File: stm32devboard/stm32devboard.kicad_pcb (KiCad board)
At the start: 4 copper layers, 20.3 x 61 mm, 44 parts, among them J1 Conn_01x20, J2 Conn_01x20, J3 USB_C_Receptacle_USB2.0, J4 Conn_01x03, SW1 SW_SPST, SW2 SW_SPST, U1 STM32F042C6Tx, U2 AP63203WU, U3 TCAN332, U4 IP4234CZ6,125

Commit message: Fixed DR fixes
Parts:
- removed J4: Conn_01x03, Connector_PinHeader_2.54mm:PinHeader_1x03_P2.54mm_Vertical
- removed JP1, JP2, JP3: Jumper_2_Open, Jumper:SolderJumper-2_P1.3mm_Open_RoundedPad1.0x1.5mm
- added C15: GCM1885C2A200JA16D, Capacitor_SMD:C_0603_1608Metric, F.Cu at (142.3, 108.6)
- added C16: GCM1885C2A200JA16D, Capacitor_SMD:C_0603_1608Metric, F.Cu at (144.7, 109.4)
- added J5: Conn_ARM_JTAG_SWD_10, Connector:Tag-Connect_TC2030-IDC-NL_2x03_P1.27mm_Vertical, F.Cu at (152.2, 89.4)
- added X1: ECS-160-10-36Q-ES-TR, Crystal:Crystal_SMD_2520-4Pin_2.5x2.0mm, F.Cu at (142.4, 106.3)
- C11: value DNP -> 0.1u
- C12: value DNP -> 1n
- R2: value 1 -> 0
- R7, R8: value 120 -> 60.4
- moved C12 10.3 mm to (144.7, 81.6), turned to 180 degrees
- moved C11 7.81 mm to (154.3, 72.9), turned to -90 degrees
- moved C8 5.41 mm to (147.0, 111.6)
- moved R3 5.32 mm to (147.0, 113.1), turned to 0 degrees
- moved R2 2.33 mm to (147.0, 110.0), turned to 0 degrees
- moved R7 1.36 mm to (144.7, 83.1)
- moved R8 1.36 mm to (141.7, 83.1)
- moved R6 0.22 mm to (142.9, 94.2), turned to 90 degrees
- turned R5 to 90 degrees
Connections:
- net LED renamed Net-(U1-PA15)
- C11 pad 1: GND -> /USB_SHLD
- C11 pad 2: CAN- -> GND
- C12 pad 2: CAN+ -> Net-(C12-Pad2)
- J2 pad 2: PF0 -> GND
- J2 pad 3: PF1 -> PF11
- J2 pad 4: PF11 -> +3V3
- R5 pad 1: Net-(U3-TXD) -> PB9
- R5 pad 2: PB9 -> Net-(U3-TXD)
- R6 pad 1: Net-(U3-RXD) -> PB8
- R6 pad 2: PB8 -> Net-(U3-RXD)
- R7 pad 1: Net-(JP1-B) -> CAN-
- R7 pad 2: GND -> Net-(C12-Pad2)
- R8 pad 1: Net-(JP2-B) -> CAN+
- R8 pad 2: GND -> Net-(C12-Pad2)
- U1 pad 34: SWDIO -> /SWDIO
- U1 pad 37: SWSCK -> /SWSCK
- U1 pad 5: PF0 -> Net-(U1-PF0)
- U1 pad 6: PF1 -> Net-(U1-PF1)
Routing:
- net PF1: track 44.0 -> 0.00 mm, vias 1 -> 0
- net PF0: track 43.0 -> 0.00 mm, vias 1 -> 0
- net GND: track 26.6 -> 41.0 mm
- net SWSCK: track 9.35 -> 0.00 mm
- net Net-(U1-PF0): track 0.00 -> 9.28 mm
- net /SWSCK: track 0.00 -> 8.98 mm
- net Net-(U1-PF1): track 0.00 -> 6.65 mm
- net /SWDIO: track 0.00 -> 6.47 mm
- net SWDIO: track 5.58 -> 0.00 mm
- net Net-(C12-Pad2): track 0.00 -> 2.94 mm
- net PF11: track 77.9 -> 75.4 mm
- net CAN+: track 20.9 -> 22.9 mm
- net Net-(JP2-B): track 2.05 -> 0.00 mm
- net Net-(JP1-B): track 2.05 -> 0.00 mm
- net /USB_SHLD: track 1.82 -> 3.74 mm
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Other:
- board text added: "3"
- board text added: "C"
- board text added: "D"
- board text added: "G"
- board text removed: "DIO"
- board text removed: "F0"
- board text removed: "F1"
- board text removed: "JS"
- board text removed: "JT"
- board text removed: "SCK"

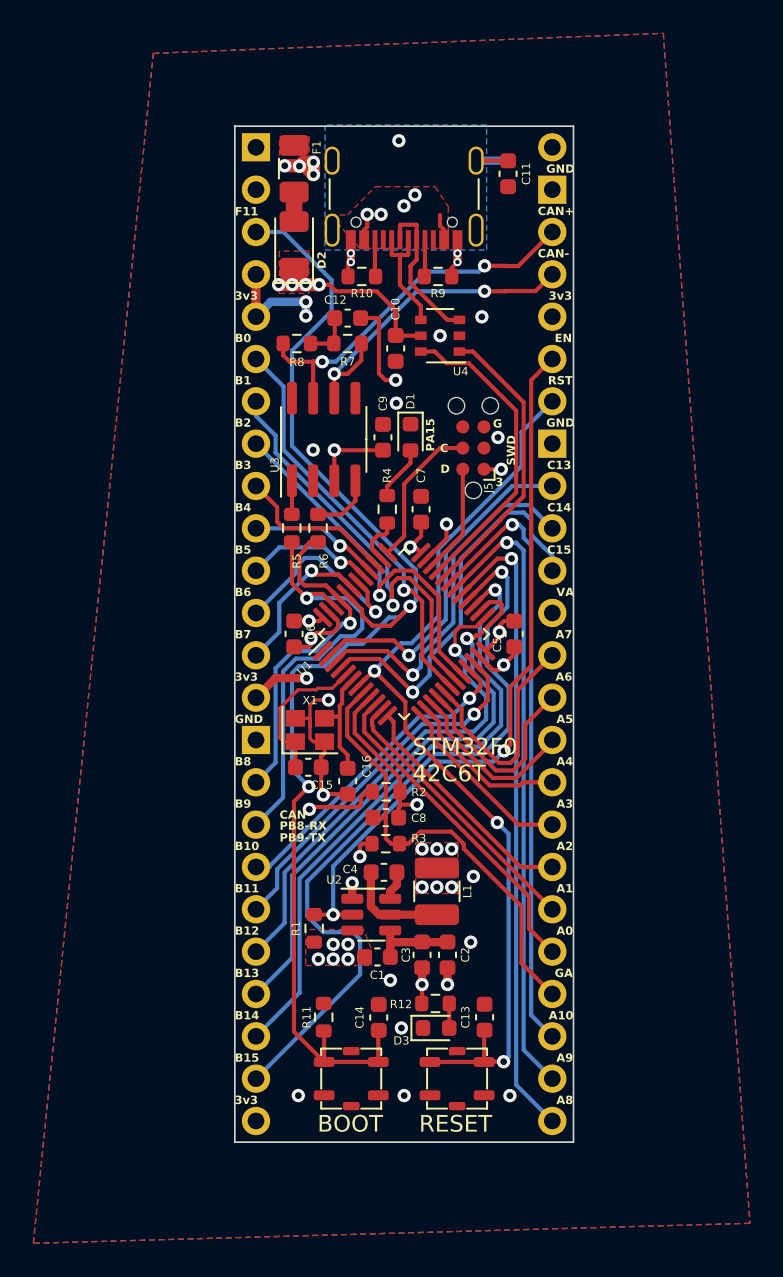
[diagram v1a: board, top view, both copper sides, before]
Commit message: Updated BOM and silkscreen
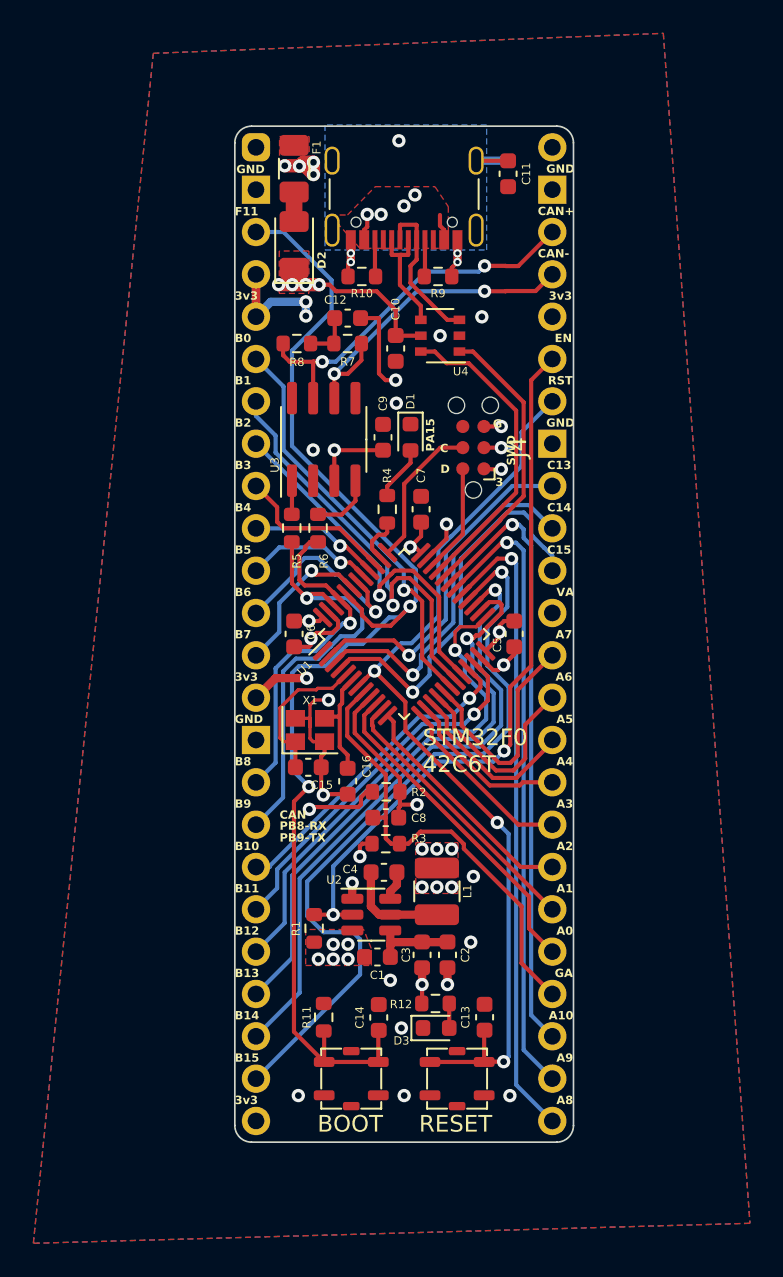
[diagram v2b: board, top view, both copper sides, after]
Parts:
- removed J5: Conn_ARM_JTAG_SWD_10, Connector:Tag-Connect_TC2030-IDC-NL_2x03_P1.27mm_Vertical
- added J4: ARM_SWD_TagConnect_TC2030-NL, Connector:Tag-Connect_TC2030-IDC-NL_2x03_P1.27mm_Vertical, F.Cu at (152.2, 89.4)
- C15, C16: value GCM1885C2A200JA16D -> 20p
- D1: value LED -> AMBER
- D3: value LED -> GREEN
- R12, R4: value 1k -> 5k1
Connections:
- net VDDA renamed +3V3A
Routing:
- net RESET: track 55.7 -> 57.9 mm, vias 3 -> 4
- net GND: track 41.0 -> 42.0 mm
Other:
- outline, holes or cut-outs redrawn
